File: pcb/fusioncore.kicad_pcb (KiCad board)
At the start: 2 copper layers, 95 x 99 mm, 102 parts, among them J1 Conn_02x12_Top_Bottom, J10 Pump_Misc_1, J11 Pump_Misc_2, J12 Flow_Warm, J13 Flow_Cold, J14 Trigger, J15 Valve_M1, J16 Valve_M2, J17 Valve_M3, J18 Valve_M4, J19 Valve_Air_Lime, J2 Temp_1, J20 Valve_Air_Rum, J21 Valve_Air_Out, J22 LED, J3 40HAT, J5 WEIGHT, J6 Pump_Water_Cold, J7 Pump_Water_Warm, J8 Pump_Air, J9 CONN_01X02, Q1 DMG2305UX, Q10 AO3400A, Q11 AO3400A, Q12 AO3400A, Q13 AO3400A, Q14 AO3400A, Q16 MMBT4403, Q2 DMMT5401, Q3 AO3400A, Q4 AO3400A, Q5 AO3400A, Q6 AO3400A, Q7 AO3400A, Q8 AO3400A, Q9 AO3400A, U1 HX711, U2 CAT24C32, U3 LTC2990, U4 LTC2990, U5 TXB0108DQSR

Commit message: Finalized current PCB iteration
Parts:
- removed J18: Valve_M4, TerminalBlock_Phoenix:TerminalBlock_Phoenix_PT-1,5-2-5.0-H_1x02_P5.00mm_Horizontal
- removed Q10, Q11, Q8, Q9: AO3400A, Package_TO_SOT_SMD:SOT-23
- removed R33: DNP, Resistor_SMD:R_0805_2012Metric_Pad1.15x1.40mm_HandSolder
- added D15: LED, Resistor_SMD:R_0603_1608Metric_Pad1.05x0.95mm_HandSolder, F.Cu at (114.1, 123.2)
- added D16: LED, Resistor_SMD:R_0603_1608Metric_Pad1.05x0.95mm_HandSolder, F.Cu at (138.0, 123.2)
- added D17: LED, Resistor_SMD:R_0603_1608Metric_Pad1.05x0.95mm_HandSolder, F.Cu at (102.0, 123.2)
- added D18: LED, Resistor_SMD:R_0603_1608Metric_Pad1.05x0.95mm_HandSolder, F.Cu at (89.9, 123.2)
- added J4: Valve_M1, TerminalBlock_Phoenix:TerminalBlock_Phoenix_PT-1,5-3-5.0-H_1x03_P5.00mm_Horizontal, F.Cu at (55.5, 89.1)
- added JP1: SolderJumper_2_Open, Jumper:SolderJumper-2_P1.3mm_Open_Pad1.0x1.5mm, F.Cu at (121.5, 75.1)
- added JP2: SolderJumper_2_Open, Jumper:SolderJumper-2_P1.3mm_Open_Pad1.0x1.5mm, F.Cu at (84.2, 74.3)
- added R10: 360, Resistor_SMD:R_0603_1608Metric_Pad1.05x0.95mm_HandSolder, F.Cu at (66.2, 126.3)
- added R34: 360, Resistor_SMD:R_0603_1608Metric_Pad1.05x0.95mm_HandSolder, F.Cu at (64.0, 120.1)
- added R35: 360, Resistor_SMD:R_0603_1608Metric_Pad1.05x0.95mm_HandSolder, F.Cu at (124.4, 123.2)
- added R36: 360, Resistor_SMD:R_0603_1608Metric_Pad1.05x0.95mm_HandSolder, F.Cu at (112.4, 123.2)
- added R37: 360, Resistor_SMD:R_0603_1608Metric_Pad1.05x0.95mm_HandSolder, F.Cu at (136.4, 123.2)
- added R38: 360, Resistor_SMD:R_0603_1608Metric_Pad1.05x0.95mm_HandSolder, F.Cu at (100.3, 123.2)
- added R39: 360, Resistor_SMD:R_0603_1608Metric_Pad1.05x0.95mm_HandSolder, F.Cu at (88.2, 123.2)
- added R9: 360, Resistor_SMD:R_0603_1608Metric_Pad1.05x0.95mm_HandSolder, F.Cu at (64.2, 107.5)
- D1, D2, D3, D4: value D -> LED; footprint Diode_SMD:D_SOD-123F -> Resistor_SMD:R_0603_1608Metric_Pad1.05x0.95mm_HandSolder
- D13: value POWER GOOD -> PWG
- D14: value STANDBY -> STB
- J15: value Valve_M1 -> Valve_M2; footprint TerminalBlock_Phoenix:TerminalBlock_Phoenix_PT-1,5-2-5.0-H_1x02_P5.00mm_Horizontal -> TerminalBlock_Phoenix:TerminalBlock_Phoenix_PT-1,5-3-5.0-H_1x03_P5.00mm_Horizontal
- J16: value Valve_M2 -> Valve_M3; footprint TerminalBlock_Phoenix:TerminalBlock_Phoenix_PT-1,5-2-5.0-H_1x02_P5.00mm_Horizontal -> TerminalBlock_Phoenix:TerminalBlock_Phoenix_PT-1,5-3-5.0-H_1x03_P5.00mm_Horizontal
- J17: value Valve_M3 -> Valve_M4; footprint TerminalBlock_Phoenix:TerminalBlock_Phoenix_PT-1,5-2-5.0-H_1x02_P5.00mm_Horizontal -> TerminalBlock_Phoenix:TerminalBlock_Phoenix_PT-1,5-3-5.0-H_1x03_P5.00mm_Horizontal
- J2: value Temp_1 -> Temperature
- J6: value Pump_Water_Cold -> Pump_Cold
- J7: value Pump_Water_Warm -> Pump_Warm
- R11: value DNP -> 10K
- R16: footprint Resistor_SMD:R_2512_6332Metric_Pad1.52x3.35mm_HandSolder -> Resistor_SMD:R_1206_3216Metric_Pad1.42x1.75mm_HandSolder
- TP1, TP2, TP3, TP4, TP5: footprint TestPoint:TestPoint_Plated_Hole_D2.0mm -> TestPoint:TestPoint_THTPad_D2.0mm_Drill1.0mm
- moved D4 87.8 mm to (126.1, 123.2), turned to 90 degrees
- moved U5 58.9 mm to (68.8, 72.6), turned to 180 degrees
- moved R11 52.8 mm to (68.9, 69.0)
- moved D3 46.5 mm to (64.0, 118.3)
- moved D2 43.1 mm to (62.7, 126.3)
- moved J16 27.9 mm to (55.5, 55.5)
- moved J17 26.0 mm to (62.3, 46.7), turned to 180 degrees
- moved J15 22.8 mm to (55.5, 72.3)
- moved D1 14.5 mm to (64.2, 109.2)
- moved R3 12.2 mm to (86.1, 54.5), turned to 0 degrees
- moved R2 3.91 mm to (69.7, 54.7), turned to 180 degrees
- moved TP5 2.62 mm to (101.9, 113.5)
- moved R21 2.57 mm to (86.4, 115.4)
- moved R22 2.57 mm to (88.4, 115.4)
- moved D7 1.99 mm to (64.1, 116.2)
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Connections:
- D1 pad 1: /12V -> Net-(D1-Pad1)
- D2 pad 1: /12V -> Net-(D2-Pad1)
- D3 pad 1: /12V -> Net-(D3-Pad1)
- D4 pad 1: /12V -> Net-(D4-Pad1)
- D5 pad 2: Net-(D5-Pad2) -> Net-(D1-Pad1)
- D6 pad 2: Net-(D6-Pad2) -> Net-(D2-Pad1)
- D7 pad 2: Net-(D7-Pad2) -> Net-(D3-Pad1)
- D8 pad 2: Net-(D8-Pad2) -> Net-(D4-Pad1)
- J15 pad 1: /12V -> GND
- J15 pad 2: Net-(D1-Pad2) -> /Valve_M2_5V
- J16 pad 1: /12V -> GND
- J16 pad 2: Net-(D2-Pad2) -> /Valve_M3_5V
- J17 pad 1: /12V -> GND
- J17 pad 2: Net-(D3-Pad2) -> /Valve_M4_5V
- J19 pad 2: Net-(D5-Pad2) -> Net-(D1-Pad1)
- J20 pad 2: Net-(D6-Pad2) -> Net-(D2-Pad1)
- J21 pad 2: Net-(D7-Pad2) -> Net-(D3-Pad1)
- J6 pad 2: Net-(D8-Pad2) -> Net-(D4-Pad1)
- Q12 pad 3: Net-(D5-Pad2) -> Net-(D1-Pad1)
- Q13 pad 3: Net-(D6-Pad2) -> Net-(D2-Pad1)
- Q14 pad 3: Net-(D7-Pad2) -> Net-(D3-Pad1)
- Q3 pad 3: Net-(D8-Pad2) -> Net-(D4-Pad1)
- R11 pad 1: Net-(J9-Pad2) -> GND
- R11 pad 2: GND -> /3V3
- U5 pad 1: /LED_PWM -> /Valve_M1
- U5 pad 10: (no net) -> /LED_PWM
- U5 pad 11: (no net) -> /LED_PWM_5V
- U5 pad 12: (no net) -> /Flow_C_5V
- U5 pad 13: (no net) -> /Flow_W_5V
- U5 pad 17: (no net) -> /Valve_M4_5V
- U5 pad 18: /Flow_C_5V -> /Valve_M3_5V
- U5 pad 19: /Flow_W_5V -> /Valve_M2_5V
- U5 pad 2: /Flow_W -> /Valve_M2
- U5 pad 20: /LED_PWM_5V -> /Valve_M1_5V
- U5 pad 3: /Flow_C -> /Valve_M3
- U5 pad 4: (no net) -> /Valve_M4
- U5 pad 6: (no net) -> /3V3
- U5 pad 8: (no net) -> /Flow_W
- U5 pad 9: (no net) -> /Flow_C
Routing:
- net /LED_PWM_5V: track 0.00 -> 58.7 mm, vias 0 -> 2
- net GND: track 168.0 -> 225.4 mm, vias 24 -> 26
- net /3V3_PI: track 183.3 -> 129.3 mm, vias 5 -> 3
- net /Flow_C_5V: track 0.00 -> 47.3 mm, vias 0 -> 2
- net /Valve_M4_5V: track 0.00 -> 35.9 mm
- net /Flow_W_5V: track 0.00 -> 30.0 mm
- net /Valve_M1_5V: track 0.00 -> 28.2 mm
- net /LED_PWM: track 20.8 -> 48.8 mm, vias 0 -> 3
- net Net-(D2-Pad1): track 0.00 -> 27.0 mm
- net Net-(D6-Pad2): track 26.9 -> 0.00 mm
- net /Valve_M3_5V: track 0.00 -> 18.9 mm
- net Net-(D1-Pad1): track 0.00 -> 16.9 mm
- net /Trigger: track 9.28 -> 26.1 mm, vias 0 -> 1
- net Net-(D3-Pad1): track 0.00 -> 16.4 mm
- net Net-(D4-Pad1): track 0.00 -> 15.9 mm
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- added copper zone on B.Cu, net /5V

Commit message: Fixed some more issues on pcb
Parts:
- D1, D15, D16, D17, D18, D2, D3, D4: footprint Resistor_SMD:R_0603_1608Metric_Pad1.05x0.95mm_HandSolder -> LED_SMD:LED_0603_1608Metric_Pad1.05x0.95mm_HandSolder
- U5: footprint Package_SON:USON-20_2x4mm_P0.4mm -> Package_SO:TSSOP-20_4.4x6.5mm_P0.65mm
- moved R11 8.29 mm to (68.5, 77.3)
- moved U5 2.39 mm to (66.4, 72.6)
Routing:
- net GND: track 225.4 -> 237.9 mm, vias 26 -> 25
- net /Valve_M2_5V: track 13.8 -> 8.96 mm
- net /Valve_M1_5V: track 28.2 -> 24.4 mm
- net /3V3: track 151.3 -> 152.9 mm
- net /5V: track 143.2 -> 141.6 mm
- net /Valve_M4_5V: track 35.9 -> 34.4 mm
- net /Valve_M3_5V: track 18.9 -> 17.5 mm
- net /Valve_M1: track 54.5 -> 53.6 mm
- net /Valve_M2: track 52.8 -> 52.2 mm

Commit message: Fixed minor issues
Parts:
- moved TP1 1.93 mm to (138.3, 89.1)
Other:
- board text added: "Fusioncore Main - Mk 1 https://tschunk.bot/"
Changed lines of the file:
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@@
   (general
     (thickness 1.6)
-    (drawings 53)
+    (drawings 54)
     (tracks 1191)
     (zones 0)
@@
       (psa4output false)
       (plotreference true)
-      (plotvalue false)
+      (plotvalue true)
       (plotinvisibletext false)
       (padsonsilk true)
@@
       (drillshape 0)
       (scaleselection 1)
-      (outputdirectory "gerber"))
+      (outputdirectory "assembly/"))
   )
   (net 0 "")
@@
     (tags "LED handsolder")
     (attr smd)
-    (fp_text reference D18 (at 0 -1.43 90) (layer F.SilkS)
+    (fp_text reference D18 (at 2.4892 0.508 180) (layer F.SilkS)
       (effects (font (size 1 1) (thickness 0.15)))
     )
-    (fp_text value LED (at 0 1.43 90) (layer F.Fab)
+    (fp_text value LED (at 0 1.43 90) (layer F.Fab) hide
       (effects (font (size 1 1) (thickness 0.15)))
     )
@@
     (tags "LED handsolder")
     (attr smd)
-    (fp_text reference D17 (at 0 -1.43 90) (layer F.SilkS)
+    (fp_text reference D17 (at 3.0988 0 90) (layer F.SilkS)
       (effects (font (size 1 1) (thickness 0.15)))
     )
-    (fp_text value LED (at 0 1.43 90) (layer F.Fab)
+    (fp_text value LED (at 0 1.43 90) (layer F.Fab) hide
       (effects (font (size 1 1) (thickness 0.15)))
     )
@@
     (tags "LED handsolder")
     (attr smd)
-    (fp_text reference D16 (at 0 -1.43 90) (layer F.SilkS)
+    (fp_text reference D16 (at 3.2004 0.0254 90) (layer F.SilkS)
       (effects (font (size 1 1) (thickness 0.15)))
     )
-    (fp_text value LED (at 0 1.43 90) (layer F.Fab)
+    (fp_text value LED (at 0 1.43 90) (layer F.Fab) hide
       (effects (font (size 1 1) (thickness 0.15)))
     )
@@
     (tags "LED handsolder")
     (attr smd)
-    (fp_text reference D15 (at 0 -1.43 90) (layer F.SilkS)
+    (fp_text reference D15 (at 3.2004 0.0254 90) (layer F.SilkS)
       (effects (font (size 1 1) (thickness 0.15)))
     )
-    (fp_text value LED (at 0 1.43 90) (layer F.Fab)
+    (fp_text value LED (at 0 1.43 90) (layer F.Fab) hide
       (effects (font (size 1 1) (thickness 0.15)))
     )
@@
     (tags "LED handsolder")
     (attr smd)
-    (fp_text reference D4 (at 0 -1.43 90) (layer F.SilkS)
+    (fp_text reference D4 (at 2.6924 0.0254 90) (layer F.SilkS)
       (effects (font (size 1 1) (thickness 0.15)))
     )
-    (fp_text value LED (at 0 1.43 90) (layer F.Fab)
+    (fp_text value LED (at 0 1.43 90) (layer F.Fab) hide
       (effects (font (size 1 1) (thickness 0.15)))
     )
@@
     (tags "LED handsolder")
     (attr smd)
-    (fp_text reference D3 (at 0 -1.43) (layer F.SilkS)
+    (fp_text reference D3 (at 2.5908 -0.0254) (layer F.SilkS)
       (effects (font (size 1 1) (thickness 0.15)))
     )
-    (fp_text value LED (at 0 1.43) (layer F.Fab)
+    (fp_text value LED (at 0 1.43) (layer F.Fab) hide
       (effects (font (size 1 1) (thickness 0.15)))
     )
@@
       (effects (font (size 1 1) (thickness 0.15)))
     )
-    (fp_text value LED (at 0 1.43) (layer F.Fab)
+    (fp_text value LED (at 0 1.43) (layer F.Fab) hide
       (effects (font (size 1 1) (thickness 0.15)))
     )
@@
     (tags "LED handsolder")
     (attr smd)
-    (fp_text reference D1 (at 0 -1.43) (layer F.SilkS)
+    (fp_text reference D1 (at 2.7178 0) (layer F.SilkS)
       (effects (font (size 1 1) (thickness 0.15)))
     )
@@
   )
   (module TestPoint:TestPoint_THTPad_D2.0mm_Drill1.0mm (layer F.Cu)
-    (at 138.325 87.1716 90)
+    (at 138.325 89.1032 90)
     (descr "THT pad as test Point, diameter 2.0mm, hole diameter 1.0mm")
     (tags "test point THT pad")
@@
       (effects (font (size 1 1) (thickness 0.15)))
     )
-    (fp_text value D (at 0 2.1) (layer F.Fab)
+    (fp_text value D (at 0 2.1) (layer F.Fab) hide
       (effects (font (size 1 1) (thickness 0.15)))
     )
@@
     (tags "capacitor handsolder")
     (attr smd)
-    (fp_text reference C5 (at 0 -1.65 90) (layer F.SilkS)
+    (fp_text reference C5 (at -0.0164 1.8796 180) (layer F.SilkS)
       (effects (font (size 1 1) (thickness 0.15)))
     )
@@
     )
   )
+  (gr_text "Fusioncore Main - Mk 1\nhttps://tschunk.bot/" (at 140.5636 76.8096 90) (layer F.SilkS)
+    (effects (font (size 1 1) (thickness 0.15)))
+  )
   (gr_line (start 85.09 60.96) (end 93.98 69.85) (layer B.SilkS) (width 0.15))

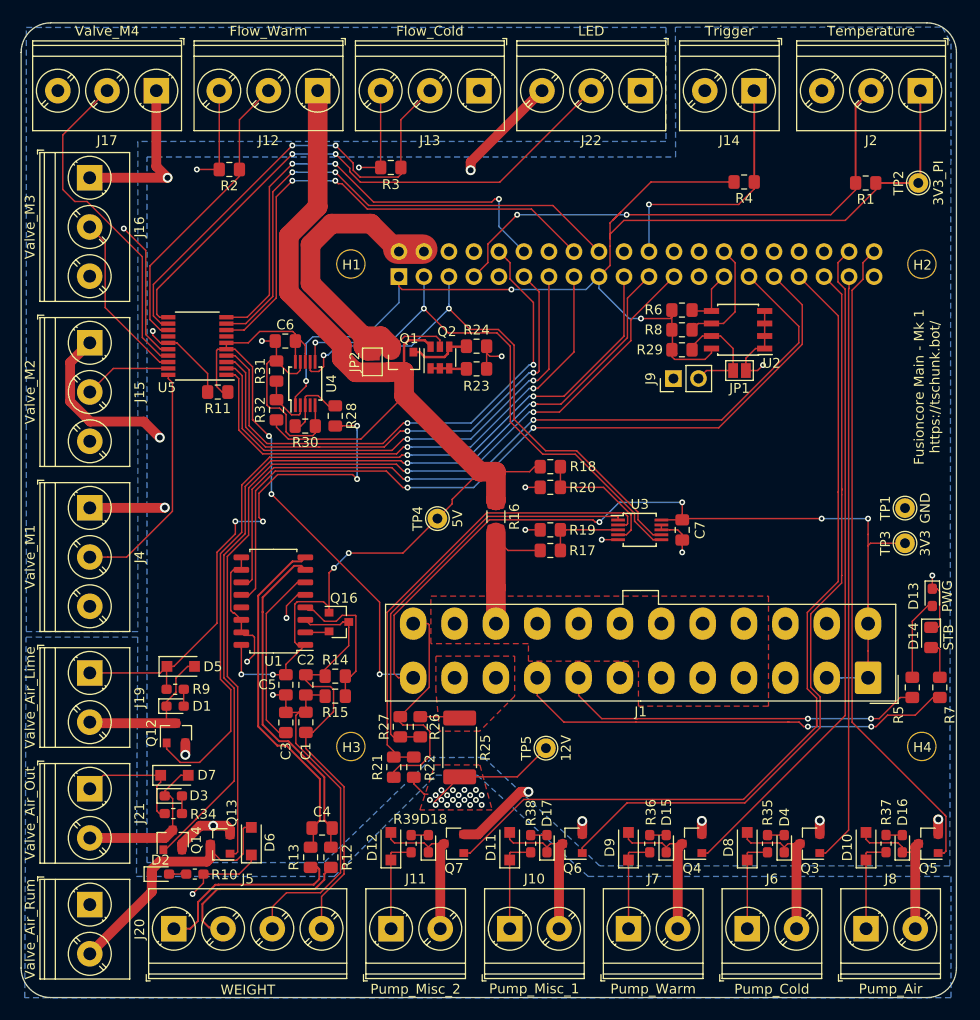
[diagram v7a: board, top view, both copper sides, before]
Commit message: Added more debug and expansion connectors
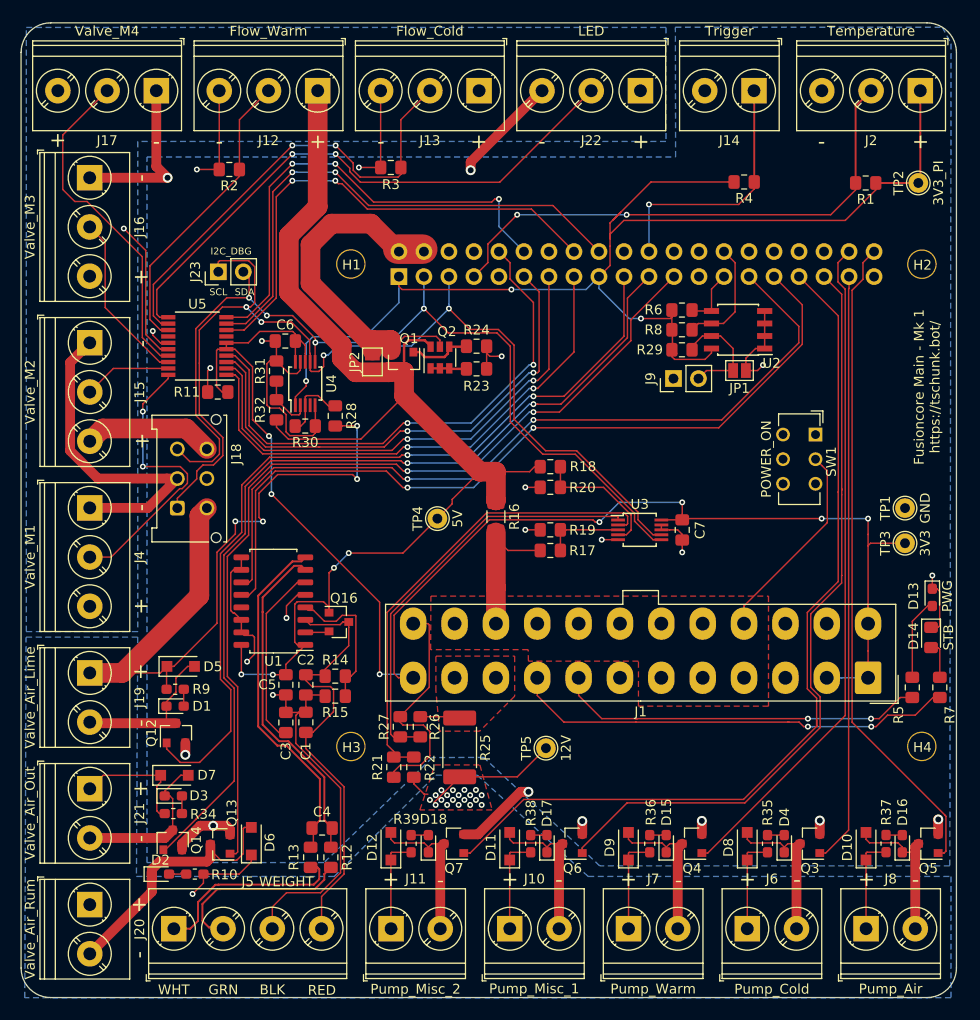
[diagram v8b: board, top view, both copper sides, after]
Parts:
- added J18: Conn_02x03_Top_Bottom, Connector_Molex:Molex_Micro-Fit_3.0_43045-0612_2x03_P3.00mm_Vertical, F.Cu at (64.4, 89.1)
- added J23: I2C_DBG, Connector_PinHeader_2.54mm:PinHeader_1x02_P2.54mm_Vertical, F.Cu at (68.6, 65.1)
- added SW1: POWER_ON, Button_Switch_THT:SW_CuK_JS202011CQN_DPDT_Straight, F.Cu at (129.2, 81.6)
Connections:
- J1 pad 16: (no net) -> /PS_ON
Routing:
- net /I2C_SCL: track 57.5 -> 104.6 mm, vias 2 -> 4
- net /I2C_SDA: track 56.5 -> 93.8 mm, vias 2 -> 4
- net /12V: track 140.2 -> 163.8 mm
- net /PS_ON: track 0.00 -> 20.7 mm
- net /5V: track 141.6 -> 154.9 mm
- net /Valve_M1_5V: track 24.4 -> 29.2 mm, vias 0 -> 2
- net GND: track 237.9 -> 242.2 mm, vias 25 -> 24
- net /5V_PI: track 38.1 -> 37.4 mm
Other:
- board text added: "+"
- board text added: "-"
- board text added: "BLK"
- board text added: "GRN"
- board text added: "RED"
- board text added: "SCL"
- board text added: "SDA"
- board text added: "WHT"
